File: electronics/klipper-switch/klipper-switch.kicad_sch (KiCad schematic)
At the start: 0 parts

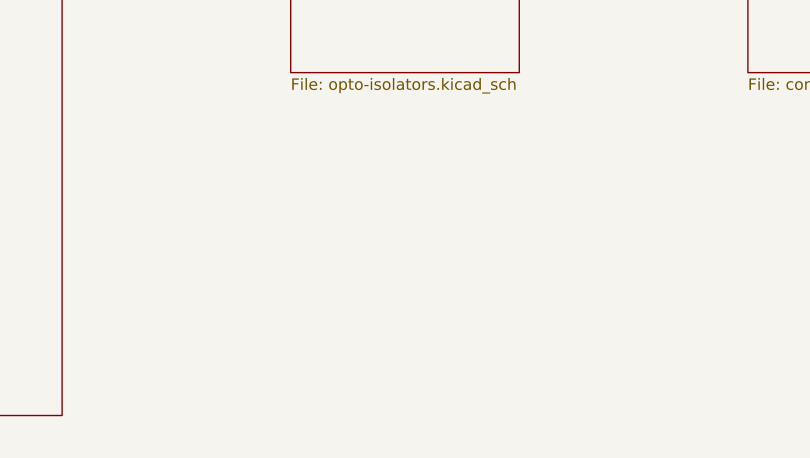
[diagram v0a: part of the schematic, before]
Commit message: output conn adjusted
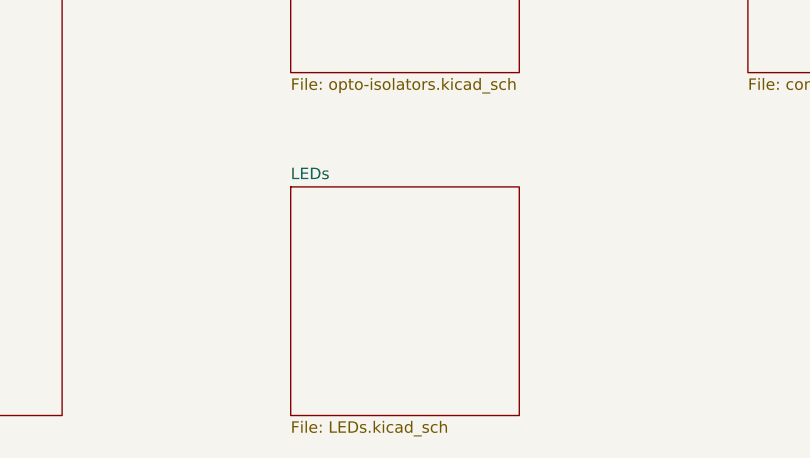
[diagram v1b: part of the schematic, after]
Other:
- added sheet LEDs (LEDs.kicad_sch)
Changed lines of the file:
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@@
+	)
+	(sheet
+		(at 76.2 152.4)
+		(size 25.4 25.4)
+		(fields_autoplaced yes)
+		(stroke
+			(width 0.1524)
+			(type solid)
+		)
+		(fill
+			(color 0 0 0 0.0000)
+		)
+		(property "Sheetname" "LEDs"
+			(at 76.2 151.6884 0)
+			(effects
+				(font
+					(size 1.27 1.27)
+				)
+				(justify left bottom)
+			)
+		)
+		(property "Sheetfile" "LEDs.kicad_sch"
+			(at 76.2 178.3846 0)
+			(effects
+				(font
+					(size 1.27 1.27)
+				)
+				(justify left top)
+			)
+		)
+		(instances
+			(project "klipper-switch"
+				(path "/e5df92b1-e048-41e8-96e5-ed9a12dbef0e"
+					(page "6")
+				)
+			)
+		)
 	)
 	(sheet
